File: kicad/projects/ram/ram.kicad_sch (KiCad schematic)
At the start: 18 parts, among them J1 peripheral_addr_bus_connector, J2 peripheral_aux_connector, J3 peripheral_membank_connector, U1 74HC02, U2 74HC08, U3 74HC123, U4 74HC04, U5 74HC245, U6 74HC245, U7 628128_DIP32_SSOP32, U8 628128_DIP32_SSOP32

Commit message: RAM schematic 80 percent complete and initial layout of PCB.
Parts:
- added C10, C11, C12, C13, C3, C4, C5, C6, C7, C8, C9: C, Capacitor_THT:C_Disc_D5.0mm_W2.5mm_P5.00mm, symbol Device:C
- added J5: Conn_02x16_Odd_Even, Connector_PinHeader_2.54mm:PinHeader_2x16_P2.54mm_Vertical, symbol Connector_Generic:Conn_02x16_Odd_Even
- added RN1, RN2: R_Network08_US, Resistor_THT:R_Array_SIP9, symbol Device:R_Network08_US
- added U10, U9: 74HC30, Package_DIP:DIP-14_W7.62mm_Socket, symbol sixteen-bit-computer:74HC30
- added U11: 74HC32, Package_DIP:DIP-14_W7.62mm_Socket, symbol sixteen-bit-computer:74HC32
- added U12: 74HC08, Package_DIP:DIP-14_W7.62mm_Socket, symbol sixteen-bit-computer:74HC08
- C1, C2: footprint (none) -> Capacitor_THT:C_Disc_D5.0mm_W2.5mm_P5.00mm
- R1, R2: footprint (none) -> Resistor_THT:R_Axial_DIN0207_L6.3mm_D2.5mm_P10.16mm_Horizontal
- U1, U2, U4: footprint (none) -> Package_DIP:DIP-14_W7.62mm_Socket
- U3: footprint (none) -> Package_DIP:DIP-16_W7.62mm_Socket
- U5, U6: footprint (none) -> Package_DIP:DIP-20_W7.62mm_Socket
- U7, U8: footprint (none) -> Package_DIP:DIP-32_W15.24mm_Socket
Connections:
- net ADDRESSED_RFM: now also U12.3
- net ADDRESSED_WTM: now also U12.6
- net ADDR_BUS_00: now also U7.12 (A0), U8.12 (A0)
- net ADDR_BUS_01: now also U7.11 (A1), U8.11 (A1)
- net ADDR_BUS_02: now also U7.10 (A2), U8.10 (A2)
- net ADDR_BUS_03: now also U7.9 (A3), U8.9 (A3)
- net ADDR_BUS_04: now also U7.8 (A4), U8.8 (A4)
- net ADDR_BUS_05: now also U7.7 (A5), U8.7 (A5)
- net ADDR_BUS_06: now also U7.6 (A6), U8.6 (A6)
- net ADDR_BUS_07: now also U7.5 (A7), U8.5 (A7)
- net ADDR_BUS_08: now also U7.27 (A8), U8.27 (A8)
- net ADDR_BUS_09: now also U7.26 (A9), U8.26 (A9)
- net ADDR_BUS_10: now also U7.23 (A10), U8.23 (A10)
- net ADDR_BUS_11: now also U7.25 (A11), U8.25 (A11)
- net ADDR_BUS_12: now also U7.4 (A12), U8.4 (A12)
- net ADDR_BUS_13: now also U7.28 (A13), U8.28 (A13)
- net ADDR_BUS_14: now also U7.3 (A14), U8.3 (A14)
- net ADDR_BUS_15: now also U7.31 (A15), U8.31 (A15)
- net BANK_BUS_00: now also J5.31 (Pin_31)
- net BANK_BUS_01: now also J5.29 (Pin_29)
- net BANK_BUS_02: now also J5.27 (Pin_27)
- net BANK_BUS_03: now also J5.25 (Pin_25)
- net BANK_BUS_04: now also J5.23 (Pin_23)
- net BANK_BUS_05: now also J5.21 (Pin_21)
- net BANK_BUS_06: now also J5.19 (Pin_19)
- net BANK_BUS_07: now also J5.17 (Pin_17)
- net BANK_BUS_08: now also J5.15 (Pin_15)
- net BANK_BUS_09: now also J5.13 (Pin_13)
- net BANK_BUS_10: now also J5.11 (Pin_11)
- net BANK_BUS_11: now also J5.9 (Pin_9)
- net BANK_BUS_12: now also J5.7 (Pin_7)
- net BANK_BUS_13: now also J5.5 (Pin_5)
- net BANK_BUS_14: now also J5.3 (Pin_3)
- net BANK_BUS_15: now also J5.1 (Pin_1)
- net DATA_BUS_00: now also U5.9 (A8)
- net DATA_BUS_01: now also U5.8 (A7)
- net DATA_BUS_02: now also U5.7 (A6)
- net DATA_BUS_03: now also U5.6 (A5)
- net DATA_BUS_04: now also U5.5 (A3)
- net DATA_BUS_05: now also U5.4 (A3)
- net DATA_BUS_06: now also U5.3 (A2)
- net DATA_BUS_07: now also U5.2 (A1)
- net DATA_BUS_08: now also U6.9 (A8)
- net DATA_BUS_09: now also U6.8 (A7)
- net DATA_BUS_10: now also U6.7 (A6)
- net DATA_BUS_11: now also U6.6 (A5)
- net DATA_BUS_12: now also U6.5 (A3)
- net DATA_BUS_13: now also U6.4 (A3)
- net DATA_BUS_14: now also U6.3 (A2)
- net DATA_BUS_15: now also U6.2 (A1)
- net GND: now also U5.10 (GND), U6.10 (GND), U7.16 (GND), U7.2 (A16), U7.22 (~{CS1}), U7.24 (~{OE}), U8.16 (GND), U8.2 (A16), U8.22 (~{CS1}), U8.24 (~{OE}), C7.1, C8.1, C9.1
- net RAM_~{WE}: now also U7.29 (~{WE}), U8.29 (~{WE})
- net RFM: now also U12.1
- net RW_BUF_DIR: now also U2.11, U4.13, U5.1 (DIR), U6.1 (DIR); no longer U2.9, U4.12
- net RW_BUF_~{OE}: now also U5.19 (~{OE}), U6.19 (~{OE})
- net VCC: now also U5.20 (VCC), U6.20 (VCC), U7.30 (CS2), U7.32 (VCC), U8.30 (CS2), U8.32 (VCC), C7.2, C8.2, C9.2, RN1.1 (common), RN2.1 (common)
- net WTM: now also U12.5
- net RAM_DATA_00: now reaches U5.11 (B8)
- net RAM_DATA_00: now also U7.13 (Q0)
- net RAM_DATA_01: now reaches U5.12 (B7)
- net RAM_DATA_01: now also U7.14 (Q1)
- net RAM_DATA_02: now reaches U5.13 (B6)
- net RAM_DATA_02: now also U7.15 (Q2)
- net RAM_DATA_03: now reaches U5.14 (B5)
- net RAM_DATA_03: now also U7.17 (Q3)
- net RAM_DATA_04: now reaches U5.15 (B4)
- net RAM_DATA_04: now also U7.18 (Q4)
- net RAM_DATA_05: now reaches U5.16 (B3)
- net RAM_DATA_05: now also U7.19 (Q5)
- net RAM_DATA_06: now reaches U5.17 (B2)
- net RAM_DATA_06: now also U7.20 (Q6)
- net RAM_DATA_07: now reaches U5.18 (B1)
- net RAM_DATA_07: now also U7.21 (Q7)
- net RAM_DATA_08: now reaches U8.13 (Q0)
- net RAM_DATA_08: now also U6.11 (B8)
- net RAM_DATA_09: now reaches U8.14 (Q1)
- net RAM_DATA_09: now also U6.12 (B7)
- net RAM_DATA_10: now reaches U8.15 (Q2)
- net RAM_DATA_10: now also U6.13 (B6)
- net RAM_DATA_11: now reaches U8.17 (Q3)
- net RAM_DATA_11: now also U6.14 (B5)
- net RAM_DATA_12: now reaches U8.18 (Q4)
- net RAM_DATA_12: now also U6.15 (B4)
- net RAM_DATA_13: now reaches U8.19 (Q5)
- net RAM_DATA_13: now also U6.16 (B3)
- net RAM_DATA_14: now reaches U8.20 (Q6)
- net RAM_DATA_14: now also U6.17 (B2)
- net RAM_DATA_15: now reaches U8.21 (Q7)
- net RAM_DATA_15: now also U6.18 (B1)
- new net: J5.18 (Pin_18), RN2.9 (R8), U10.1 (A)
- new net: J5.30 (Pin_30), RN2.3 (R2), U10.11 (G)
- new net: J5.32 (Pin_32), RN2.2 (R1), U10.12 (H)
- new net: J5.20 (Pin_20), RN2.8 (R7), U10.2 (B)
- new net: J5.22 (Pin_22), RN2.7 (R6), U10.3 (C)
- new net: J5.24 (Pin_24), RN2.6 (R5), U10.4 (D)
- new net: J5.26 (Pin_26), RN2.5 (R4), U10.5 (E)
- new net: J5.28 (Pin_28), RN2.4 (R3), U10.6 (F)
- new net: U10.8 (~{Y}), U11.2
- new net: U2.9, U4.12
- new net: U11.1, U9.8 (~{Y})
- new net: U11.3, U12.2, U12.4
- new net: J5.2 (Pin_2), RN1.2 (R1), U9.1 (A)
- new net: J5.14 (Pin_14), RN1.8 (R7), U9.11 (G)
- new net: J5.16 (Pin_16), RN1.9 (R8), U9.12 (H)
- new net: J5.4 (Pin_4), RN1.3 (R2), U9.2 (B)
- new net: J5.6 (Pin_6), RN1.4 (R3), U9.3 (C)
- new net: J5.8 (Pin_8), RN1.5 (R4), U9.4 (D)
- new net: J5.10 (Pin_10), RN1.6 (R5), U9.5 (E)
- new net: J5.12 (Pin_12), RN1.7 (R6), U9.6 (F)
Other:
- note added: "Bank selection and decoding"
- note added: "Note that this direction has been inverted compared to the physical breadboard and fritzing because the layout of the RAM and buffers on the PCB will be opposite, meaning the signals travel in the opposite direction."
- note added: "Pulse Generation"
- note added: "RAM and bus buffers"
- note added: "RAM control signal generation"
- note added: "Safe clock enable"
- moved on the sheet: C1, C2, C97, C98, C99, J1, J2, J3, R1, R2, U1A, U1B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

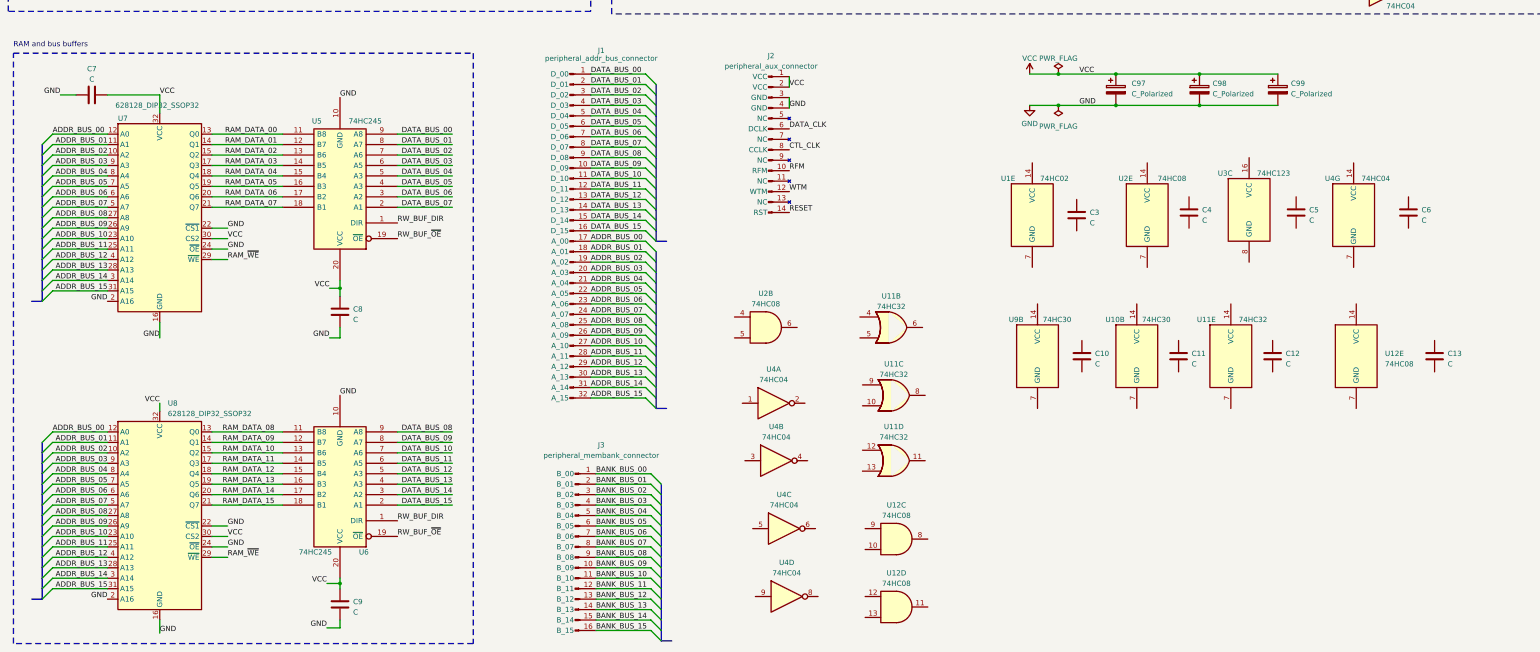
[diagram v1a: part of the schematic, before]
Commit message: Clean up some ERC checks in RAM
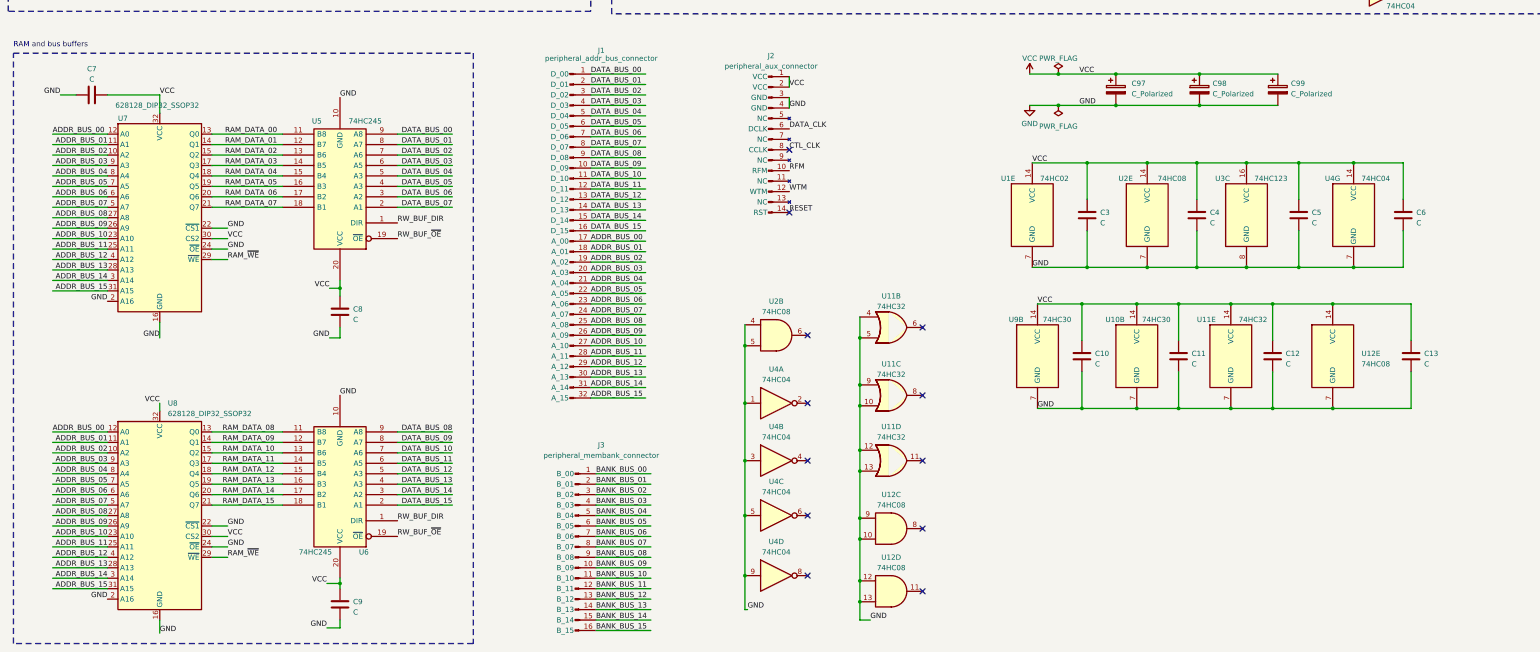
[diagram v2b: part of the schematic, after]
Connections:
- net GND: now also C10.2, C11.2, C12.2, C13.2, C3.2, C4.2, C5.2, C6.2, U1.7 (GND), U10.7 (GND), U11.10, U11.12, U11.13, U11.4, U11.5, U11.7 (GND), U11.9, U12.10, U12.12, U12.13, U12.7 (GND), U12.9, U2.4, U2.5, U2.7 (GND), U3.8 (GND), U4.1, U4.3, U4.5, U4.7 (GND), U4.9, U9.7 (GND)
- net VCC: now also C10.1, C11.1, C12.1, C13.1, C3.1, C4.1, C5.1, C6.1, U1.14 (VCC), U10.14 (VCC), U11.14 (VCC), U12.14 (VCC), U2.14 (VCC), U3.16 (VCC), U4.14 (VCC), U9.14 (VCC)
- no-connect marks 1 -> 13
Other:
- moved on the sheet: C13, C3, C4, C5, C6, U11C, U11D, U12C, U12D, U12E, U2B, U3C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

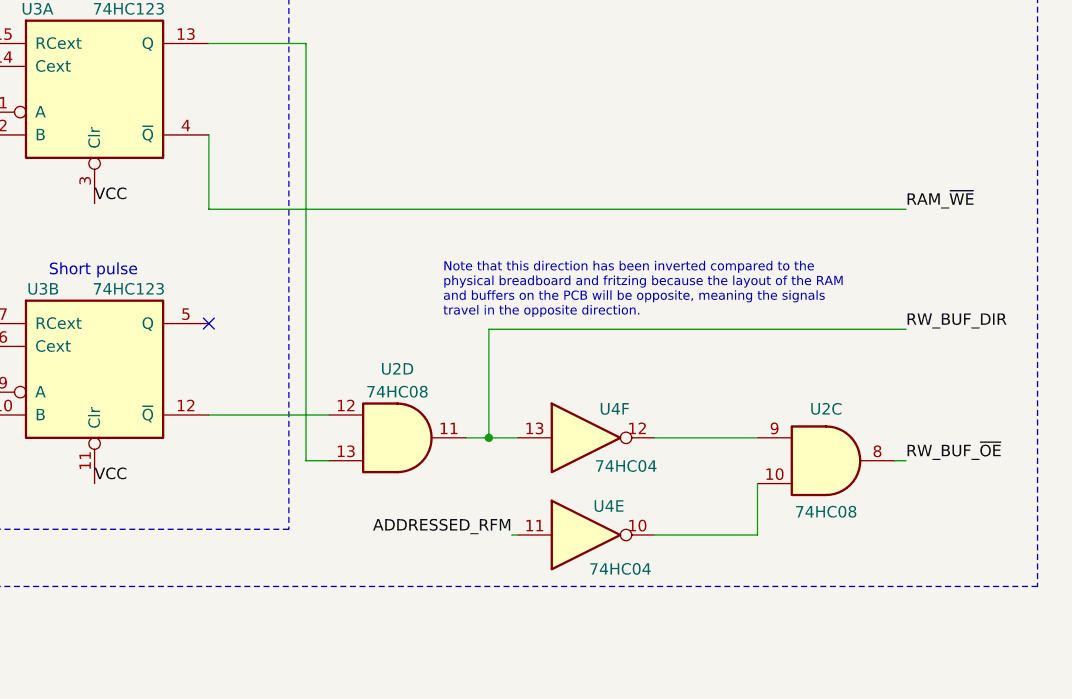
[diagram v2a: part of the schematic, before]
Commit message: Start laying out RAM wiring.
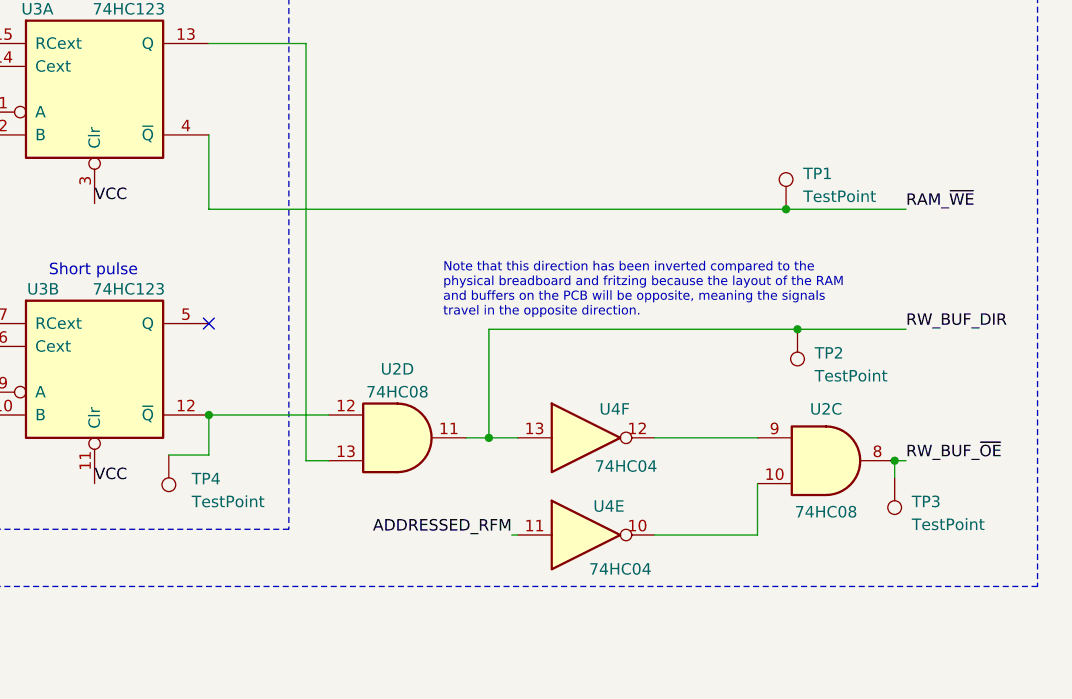
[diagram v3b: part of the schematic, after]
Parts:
- added TP1, TP2, TP3, TP4: TestPoint, Connector_PinHeader_2.54mm:PinHeader_1x01_P2.54mm_Vertical, symbol Connector:TestPoint
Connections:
- net RAM_~{WE}: now also TP1.1
- net RW_BUF_DIR: now also TP2.1
- net RW_BUF_~{OE}: now also TP3.1
- net at U2.12, U3.12 (~{Q}): now also TP4.1
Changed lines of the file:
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@@
 (kicad_sch (version 20230121) (generator eeschema)
   (paper "B")
-  (bus_alias "DATA_BUS" (members "DATA_BUS_00" "DATA_BUS_01" "DATA_BUS_02" "DATA_BUS_03" "DATA_BUS_04" "DATA_BUS_05" "DATA_BUS_06" "DATA_BUS_07" "DATA_BUS_08" "DATA_BUS_09" "DATA_BUS_10" "DATA_BUS_11" "DATA_BUS_12" "DATA_BUS_13" "DATA_BUS_14" "DATA_BUS_15"))
   (bus_alias "BANK_BUS" (members "BANK_BUS_00" "BANK_BUS_01" "BANK_BUS_02" "BANK_BUS_03" "BANK_BUS_04" "BANK_BUS_05" "BANK_BUS_06" "BANK_BUS_07" "BANK_BUS_08" "BANK_BUS_09" "BANK_BUS_10" "BANK_BUS_11" "BANK_BUS_12" "BANK_BUS_13" "BANK_BUS_14" "BANK_BUS_15"))
   (bus_alias "ADDR_BUS" (members "ADDR_BUS_00" "ADDR_BUS_01" "ADDR_BUS_02" "ADDR_BUS_03" "ADDR_BUS_04" "ADDR_BUS_05" "ADDR_BUS_06" "ADDR_BUS_07" "ADDR_BUS_08" "ADDR_BUS_09" "ADDR_BUS_10" "ADDR_BUS_11" "ADDR_BUS_12" "ADDR_BUS_13" "ADDR_BUS_14" "ADDR_BUS_15"))
+  (bus_alias "DATA_BUS" (members "DATA_BUS_00" "DATA_BUS_01" "DATA_BUS_02" "DATA_BUS_03" "DATA_BUS_04" "DATA_BUS_05" "DATA_BUS_06" "DATA_BUS_07" "DATA_BUS_08" "DATA_BUS_09" "DATA_BUS_10" "DATA_BUS_11" "DATA_BUS_12" "DATA_BUS_13" "DATA_BUS_14" "DATA_BUS_15"))
   (junction (at 69.215 74.93) (diameter 0) (color 0 0 0 0)
   )
@@
   (junction (at 227.965 182.245) (diameter 0) (color 0 0 0 0)
   )
+  (junction (at 379.095 74.93) (diameter 0) (color 0 0 0 0)
+  )
   (junction (at 200.025 240.03) (diameter 0) (color 0 0 0 0)
   )
@@
   (junction (at 342.9 173.99) (diameter 0) (color 0 0 0 0)
   )
+  (junction (at 389.89 89.535) (diameter 0) (color 0 0 0 0)
+  )
   (junction (at 328.295 199.39) (diameter 0) (color 0 0 0 0)
   )
@@
   (junction (at 276.86 71.755) (diameter 0) (color 0 0 0 0)
   )
+  (junction (at 313.69 84.455) (diameter 0) (color 0 0 0 0)
+  )
   (junction (at 227.965 198.755) (diameter 0) (color 0 0 0 0)
   )
@@
   (junction (at 227.965 246.38) (diameter 0) (color 0 0 0 0)
   )
+  (junction (at 377.825 61.595) (diameter 0) (color 0 0 0 0)
+  )
   (junction (at 328.295 173.99) (diameter 0) (color 0 0 0 0)
   )
@@
     (stroke (width 0) (type default))
   )
-  (wire (pts (xy 391.16 61.595) (xy 313.69 61.595))
+  (wire (pts (xy 391.16 61.595) (xy 377.825 61.595))
     (stroke (width 0) (type default))
   )
@@
     (stroke (width 0) (type default))
   )
+  (wire (pts (xy 313.69 88.9) (xy 313.69 84.455))
+    (stroke (width 0) (type default))
+  )
   (wire (pts (xy 200.025 198.12) (xy 200.025 212.09))
     (stroke (width 0) (type default))
@@
     (stroke (width 0) (type default))
   )
+  (wire (pts (xy 309.245 88.9) (xy 313.69 88.9))
+    (stroke (width 0) (type default))
+  )
   (wire (pts (xy 363.22 86.995) (xy 374.65 86.995))
     (stroke (width 0) (type default))
@@
     (stroke (width 0) (type default))
   )
+  (wire (pts (xy 377.825 61.595) (xy 313.69 61.595))
+    (stroke (width 0) (type default))
+  )
   (wire (pts (xy 328.295 173.99) (xy 342.9 173.99))
     (stroke (width 0) (type default))
@@
     (stroke (width 0) (type default))
   )
+  (wire (pts (xy 379.095 74.93) (xy 391.16 74.93))
+    (stroke (width 0) (type default))
+  )
   (wire (pts (xy 45.085 207.645) (xy 31.75 207.645))
     (stroke (width 0) (type default))
@@
     (stroke (width 0) (type default))
   )
+  (wire (pts (xy 389.89 89.535) (xy 389.89 91.44))
+    (stroke (width 0) (type default))
+  )
   (wire (pts (xy 69.215 46.99) (xy 88.9 46.99))
     (stroke (width 0) (type default))
@@
     (stroke (width 0) (type default))
   )
-  (wire (pts (xy 344.805 74.93) (xy 391.16 74.93))
+  (wire (pts (xy 344.805 74.93) (xy 379.095 74.93))
     (stroke (width 0) (type default))
   )
@@
     )
   )
+  (symbol (lib_id "Connector:TestPoint") (at 379.095 74.93 180) (unit 1)
+    (in_bom yes) (on_board yes) (dnp no) (fields_autoplaced)
+    (property "Reference" "TP2" (at 381 77.597 0)
+      (effects (font (size 1.27 1.27)) (justify right))
+    )
+    (property "Value" "TestPoint" (at 381 80.137 0)
+      (effects (font (size 1.27 1.27)) (justify right))
+    )
+    (property "Footprint" "Connector_PinHeader_2.54mm:PinHeader_1x01_P2.54mm_Vertical" (at 374.015 74.93 0)
+      (effects (font (size 1.27 1.27)) hide)
+    )
+    (property "Datasheet" "~" (at 374.015 74.93 0)
+      (effects (font (size 1.27 1.27)) hide)
+    )
+    (pin "1")
+    (instances
+      (project "ram"
+        (path "/0c25b387-1696-4e3f-ab8e-df646088b074"
+          (reference "TP2") (unit 1)
+        )
+      )
+    )
+  )
   (symbol (lib_id "74xx:74HC02") (at 222.25 59.69 0) (unit 2)
     (in_bom yes) (on_board yes) (dnp no)
@@
     )
   )
+  (symbol (lib_id "Connector:TestPoint") (at 377.825 61.595 0) (unit 1)
+    (in_bom yes) (on_board yes) (dnp no) (fields_autoplaced)
+    (property "Reference" "TP1" (at 379.73 57.658 0)
+      (effects (font (size 1.27 1.27)) (justify left))
+    )
+    (property "Value" "TestPoint" (at 379.73 60.198 0)
+      (effects (font (size 1.27 1.27)) (justify left))
+    )
+    (property "Footprint" "Connector_PinHeader_2.54mm:PinHeader_1x01_P2.54mm_Vertical" (at 382.905 61.595 0)
+      (effects (font (size 1.27 1.27)) hide)
+    )
+    (property "Datasheet" "~" (at 382.905 61.595 0)
+      (effects (font (size 1.27 1.27)) hide)
+    )
+    (pin "1")
+    (instances
+      (project "ram"
+        (path "/0c25b387-1696-4e3f-ab8e-df646088b074"
+          (reference "TP1") (unit 1)
+        )
+      )
+    )
+  )
   (symbol (lib_id "Connector_Generic:Conn_02x16_Odd_Even") (at 44.45 59.69 0) (unit 1)
     (in_bom yes) (on_board yes) (dnp no) (fields_autoplaced)
@@
     )
   )
+  (symbol (lib_id "Connector:TestPoint") (at 309.245 88.9 180) (unit 1)
+    (in_bom yes) (on_board yes) (dnp no) (fields_autoplaced)
+    (property "Reference" "TP4" (at 311.785 91.567 0)
+      (effects (font (size 1.27 1.27)) (justify right))
+    )
+    (property "Value" "TestPoint" (at 311.785 94.107 0)
+      (effects (font (size 1.27 1.27)) (justify right))
+    )
+    (property "Footprint" "Connector_PinHeader_2.54mm:PinHeader_1x01_P2.54mm_Vertical" (at 304.165 88.9 0)
+      (effects (font (size 1.27 1.27)) hide)
+    )
+    (property "Datasheet" "~" (at 304.165 88.9 0)
+      (effects (font (size 1.27 1.27)) hide)
+    )
+    (pin "1")
+    (instances
+      (project "ram"
+        (path "/0c25b387-1696-4e3f-ab8e-df646088b074"
+          (reference "TP4") (unit 1)
+        )
+      )
+    )
+  )
   (symbol (lib_id "sixteen-bit-computer:peripheral_aux_connector") (at 205.74 133.985 0) (unit 1)
     (in_bom yes) (on_board yes) (dnp no)
@@
         )
       )
+    )
+  )
+  (symbol (lib_id "Connector:TestPoint") (at 389.89 91.44 180) (unit 1)
+    (in_bom yes) (on_board yes) (dnp no) (fields_autoplaced)
+    (property "Reference" "TP3" (at 391.795 94.107 0)
+      (effects (font (size 1.27 1.27)) (justify right))
+    )
+    (property "Value" "TestPoint" (at 391.795 96.647 0)
+      (effects (font (size 1.27 1.27)) (justify right))
+    )
+    (property "Footprint" "Connector_PinHeader_2.54mm:PinHeader_1x01_P2.54mm_Vertical" (at 384.81 91.44 0)
+      (effects (font (size 1.27 1.27)) hide)
+    )
+    (property "Datasheet" "~" (at 384.81 91.44 0)
+      (effects (font (size 1.27 1.27)) hide)
+    )
+    (pin "1")
+    (instances
+      (project "ram"
+        (path "/0c25b387-1696-4e3f-ab8e-df646088b074"
+          (reference "TP3") (unit 1)
+        )
+      )
